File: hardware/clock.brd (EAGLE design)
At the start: 37.8 x 36.8 mm, 9 parts, among them IC2 PCF2123TSSOP14, P1 FSM4JSMA-SMD, P2 FSM4JSMA-SMD, X2 CRYSTALTFORK_SMD

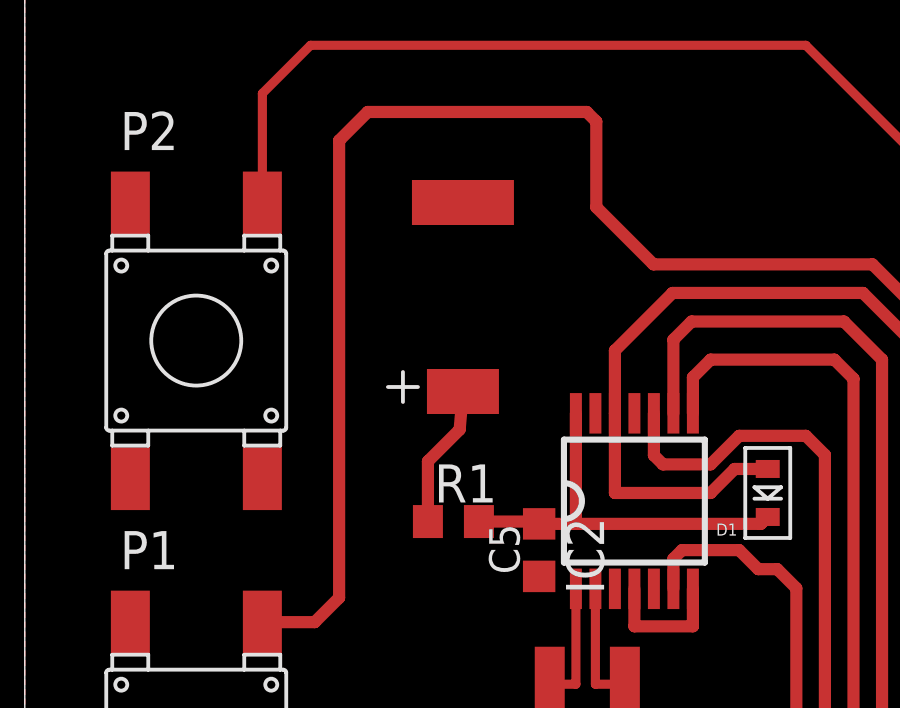
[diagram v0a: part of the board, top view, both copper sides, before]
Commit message: changed supercap to a bigger one
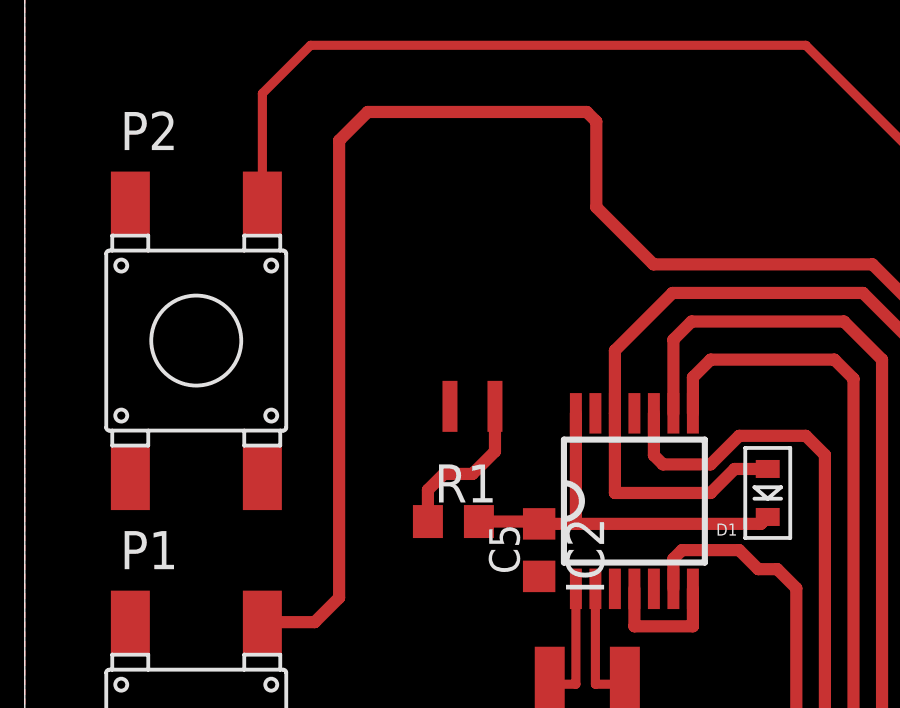
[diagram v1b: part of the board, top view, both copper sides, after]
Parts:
- removed C8: SUPERCAP414-VA5R, jocki:414-VA5R
- added U$1: DCK-3R3E224U-E, jocki:SUPCAP-E
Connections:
- removed net N$9: C8.PLUS, R1.1
- new net N$1: R1.1, U$1.+
- net GND: now also U$1.-; no longer C8.MINUS
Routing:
- net N$1: track 0.00 -> 5.32 mm
- net N$9: track 4.78 -> 0.00 mm
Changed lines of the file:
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@@
 <wire x1="37.77" y1="36.82" x2="0" y2="36.82" width="0" layer="20"/>
 <wire x1="0" y1="36.82" x2="0" y2="0" width="0" layer="20"/>
-<rectangle x1="12.065" y1="24.765" x2="17.145" y2="28.575" layer="41" rot="R180"/>
-<rectangle x1="12.065" y1="24.765" x2="17.145" y2="28.575" layer="41" rot="R270"/>
 </plain>
 <attributes>
@@
 <element name="X2" library="jocki" package="TFORK_SMD" value="CRYSTALTFORK_SMD" x="18.75" y="10.945" rot="R90"/>
 <element name="D1" library="adafruit" package="SOD-523" value="" x="24.765" y="20.32" rot="R180"/>
-<element name="C8" library="jocki" package="414-VA5R" value="SUPERCAP414-VA5R" x="14.605" y="26.3525" rot="R90"/>
 <element name="R1" library="rcl" package="R0603" value="1k" x="14.2875" y="19.3675"/>
 <element name="C5" library="rcl" package="C0603K" value="100n" x="17.145" y="18.415" rot="R90"/>
@@
 <attribute name="OC_FARNELL" value="unknown" x="34.29" y="19.05" size="1.778" layer="27" rot="R270" display="off"/>
 </element>
+<element name="U$1" library="jocki" package="SUPCAP-E" value="DCK-3R3E224U-E" x="14.9225" y="28.2575"/>
 </elements>
 <signals>
 <signal name="GND">
-<contactref element="C8" pad="MINUS"/>
-<contactref element="C5" pad="1"/>
-<contactref element="IC2" pad="7"/>
-<contactref element="IC2" pad="4"/>
-<wire x1="20.32" y1="17.125" x2="20.32" y2="15.875" width="0.4064" layer="1"/>
-<wire x1="20.32" y1="15.875" x2="22.27" y2="15.875" width="0.4064" layer="1"/>
-<wire x1="22.27" y1="15.875" x2="22.27" y2="17.125" width="0.4064" layer="1"/>
 <contactref element="P1" pad="P$1"/>
 <contactref element="P2" pad="P$1"/>
@@
 </polygon>
 <contactref element="SV1" pad="9"/>
+<contactref element="U$1" pad="-"/>
+<contactref element="C5" pad="1"/>
+<contactref element="IC2" pad="7"/>
+<wire x1="20.32" y1="15.875" x2="22.27" y2="15.875" width="0.4064" layer="1"/>
+<wire x1="22.27" y1="15.875" x2="22.27" y2="17.125" width="0.4064" layer="1"/>
+<contactref element="IC2" pad="4"/>
+<wire x1="20.32" y1="17.125" x2="20.32" y2="15.875" width="0.4064" layer="1"/>
 </signal>
 <signal name="N$3">
@@
 <wire x1="15.1375" y1="19.3675" x2="17.0675" y2="19.3675" width="0.4064" layer="1"/>
 <wire x1="17.0675" y1="19.3675" x2="17.145" y2="19.29" width="0.4064" layer="1"/>
-</signal>
-<signal name="N$9">
-<contactref element="R1" pad="1"/>
-<contactref element="C8" pad="PLUS"/>
-<wire x1="14.605" y1="23.7025" x2="14.495" y2="22.4325" width="0.4064" layer="1"/>
-<wire x1="14.495" y1="22.4325" x2="13.4375" y2="21.375" width="0.4064" layer="1"/>
-<wire x1="13.4375" y1="19.3675" x2="13.4375" y2="21.375" width="0.4064" layer="1"/>
 </signal>
 <signal name="1HZ">
@@
 <wire x1="22.86" y1="24.765" x2="26.9875" y2="24.765" width="0.4064" layer="1"/>
 </signal>
+<signal name="N$1">
+<contactref element="R1" pad="1"/>
+<contactref element="U$1" pad="+"/>
+<wire x1="13.4375" y1="19.3675" x2="13.4375" y2="20.4225" width="0.4064" layer="1"/>
+<wire x1="13.4375" y1="20.4225" x2="13.97" y2="20.955" width="0.4064" layer="1"/>
+<wire x1="13.97" y1="20.955" x2="14.9225" y2="20.955" width="0.4064" layer="1"/>
+<wire x1="14.9225" y1="20.955" x2="15.6725" y2="21.705" width="0.4064" layer="1"/>
+<wire x1="15.6725" y1="23.2075" x2="15.6725" y2="21.705" width="0.4064" layer="1"/>
+</signal>
 </signals>
